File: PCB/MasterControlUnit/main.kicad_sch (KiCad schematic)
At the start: 18 parts, among them J3 An-IN, U1 STM32F407G-DISC1, U15 MCP23017_SO, U17 ADA4096-2ARMZ, U5 LD1117S33TR_SOT223

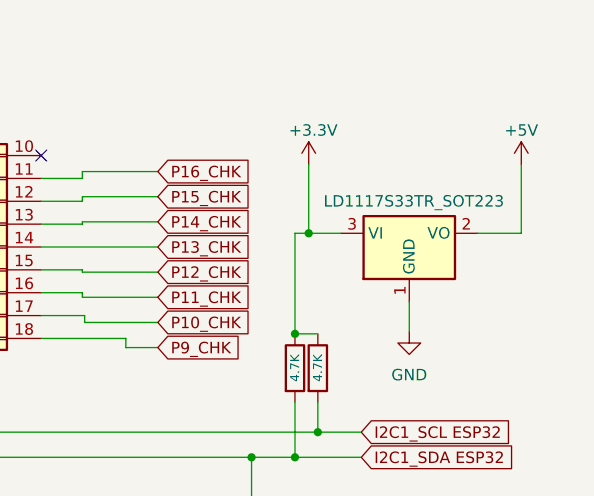
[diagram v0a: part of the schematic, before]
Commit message: Fixes for HILO's PCB sheme
Electrolitic capacitors added for 3.3V and 5V electric power stability
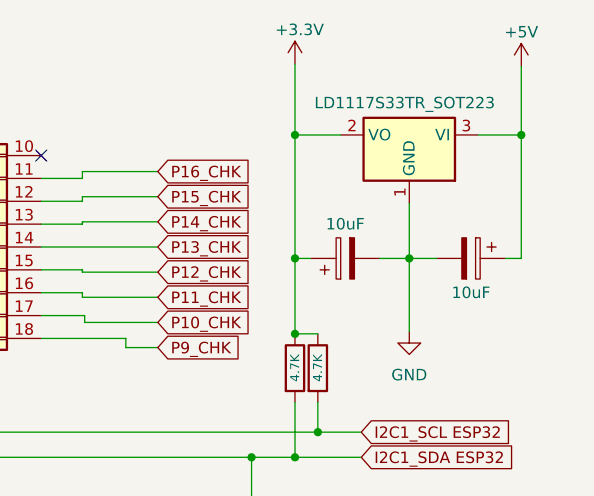
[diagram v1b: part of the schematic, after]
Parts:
- added C13, C14: 10uF, Capacitor_THT:C_Radial_D5.0mm_H7.0mm_P2.00mm, symbol Device:C_Polarized
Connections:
- net +3.3V: now also U5.2 (VO), C13.1; no longer U5.3 (VI)
- net +5V: now also U5.3 (VI), C14.1; no longer U5.2 (VO)
- net GND: now also C13.2, C14.2
